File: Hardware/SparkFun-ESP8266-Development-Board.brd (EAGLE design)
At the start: 55.3 x 25.9 mm, 73 parts, among them J1 U.FL, Q1 2.5A/30V, U1 ESP8266, U2 MCP73831, U3 AT25SF041-SOIC8, U4 AP2112K-3.3V, U5 ATECC108-MAHDA, U6 TMP1021:1, U7 TSL2561FN, Y1 26MHz

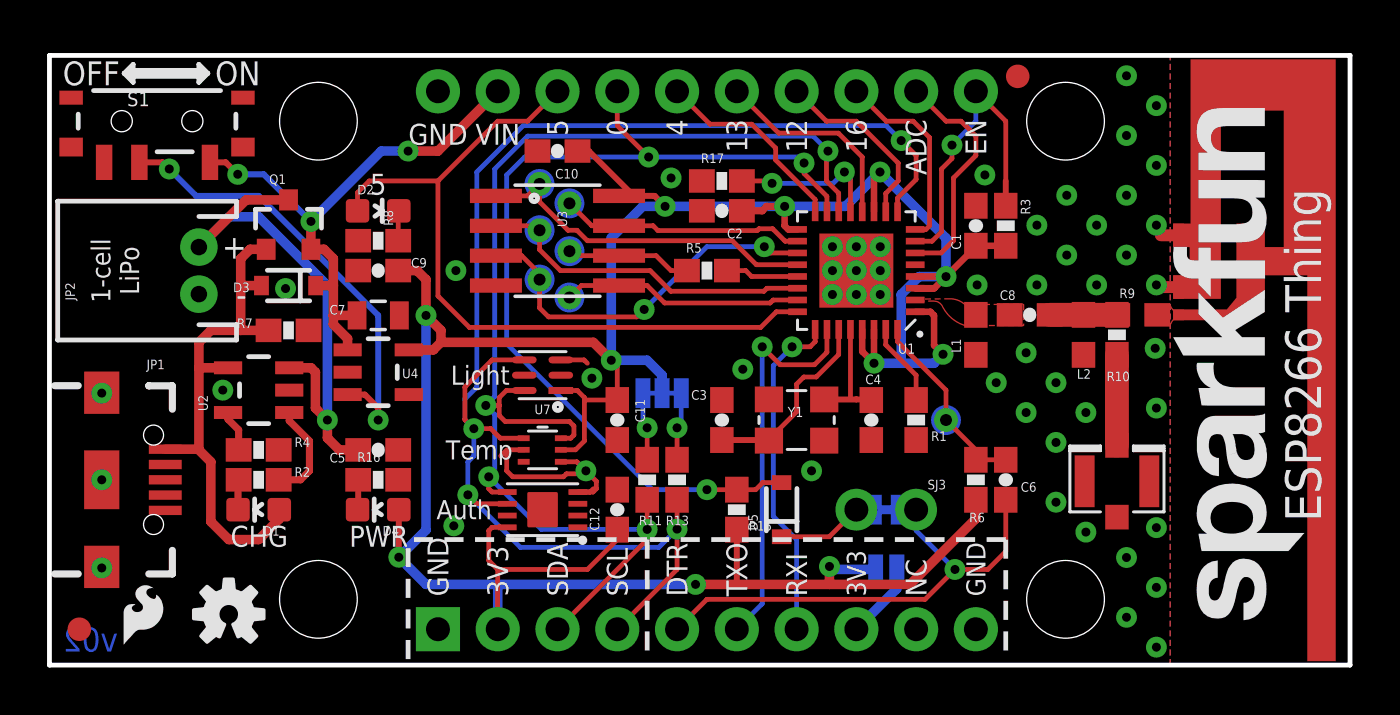
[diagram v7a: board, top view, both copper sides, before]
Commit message: Revising silkscreen. Optimizing some traces. Updated to v10.
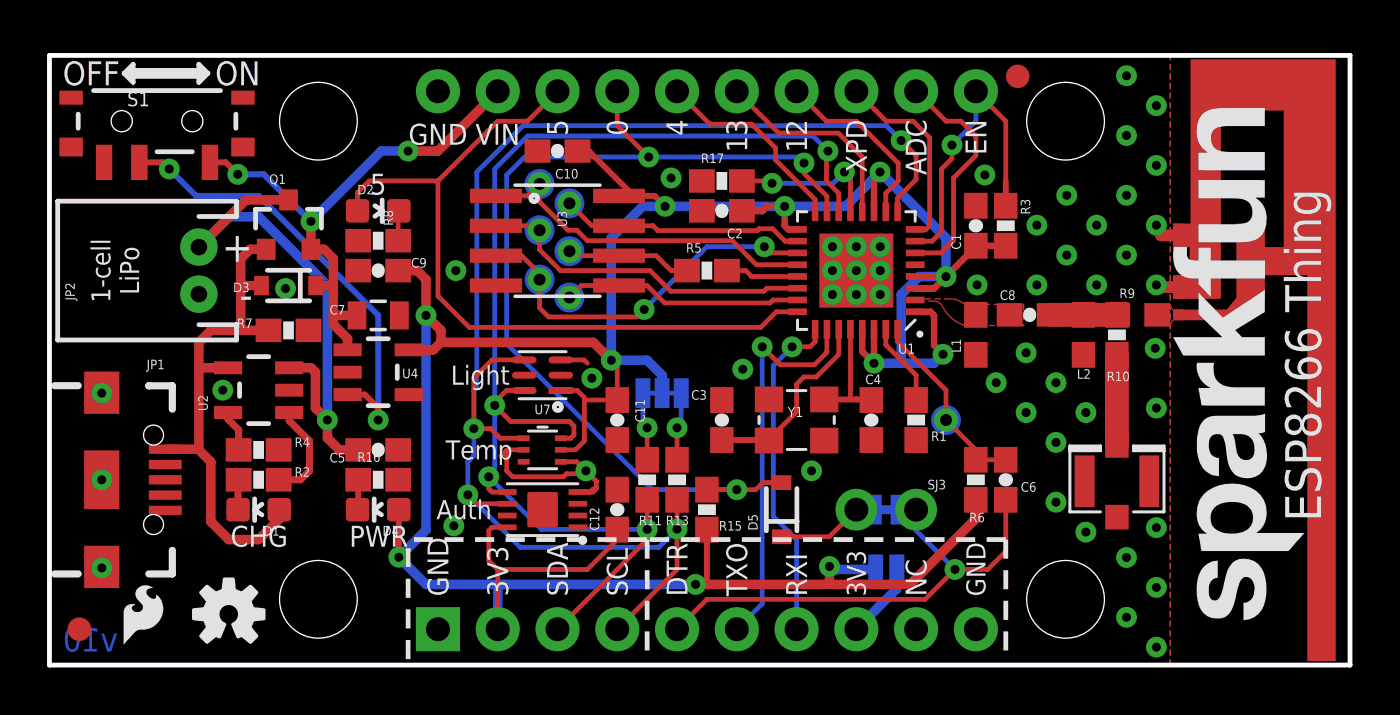
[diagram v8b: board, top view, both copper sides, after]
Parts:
- moved R15 1.27 mm to (27.9, 6.35)
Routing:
- net GPIO0: track 40.4 -> 41.7 mm
- net GPIO2/SDA: track 54.3 -> 53.4 mm
- net GPIO14/SCL: track 62.7 -> 62.0 mm
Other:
- board text added: "XPD"
- board text added: "v10"
- board text removed: "16"
- board text removed: "v02"
